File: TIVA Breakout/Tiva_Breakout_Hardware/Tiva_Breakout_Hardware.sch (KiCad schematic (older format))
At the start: 60 parts, among them U1 TM4C129E_Launchpad

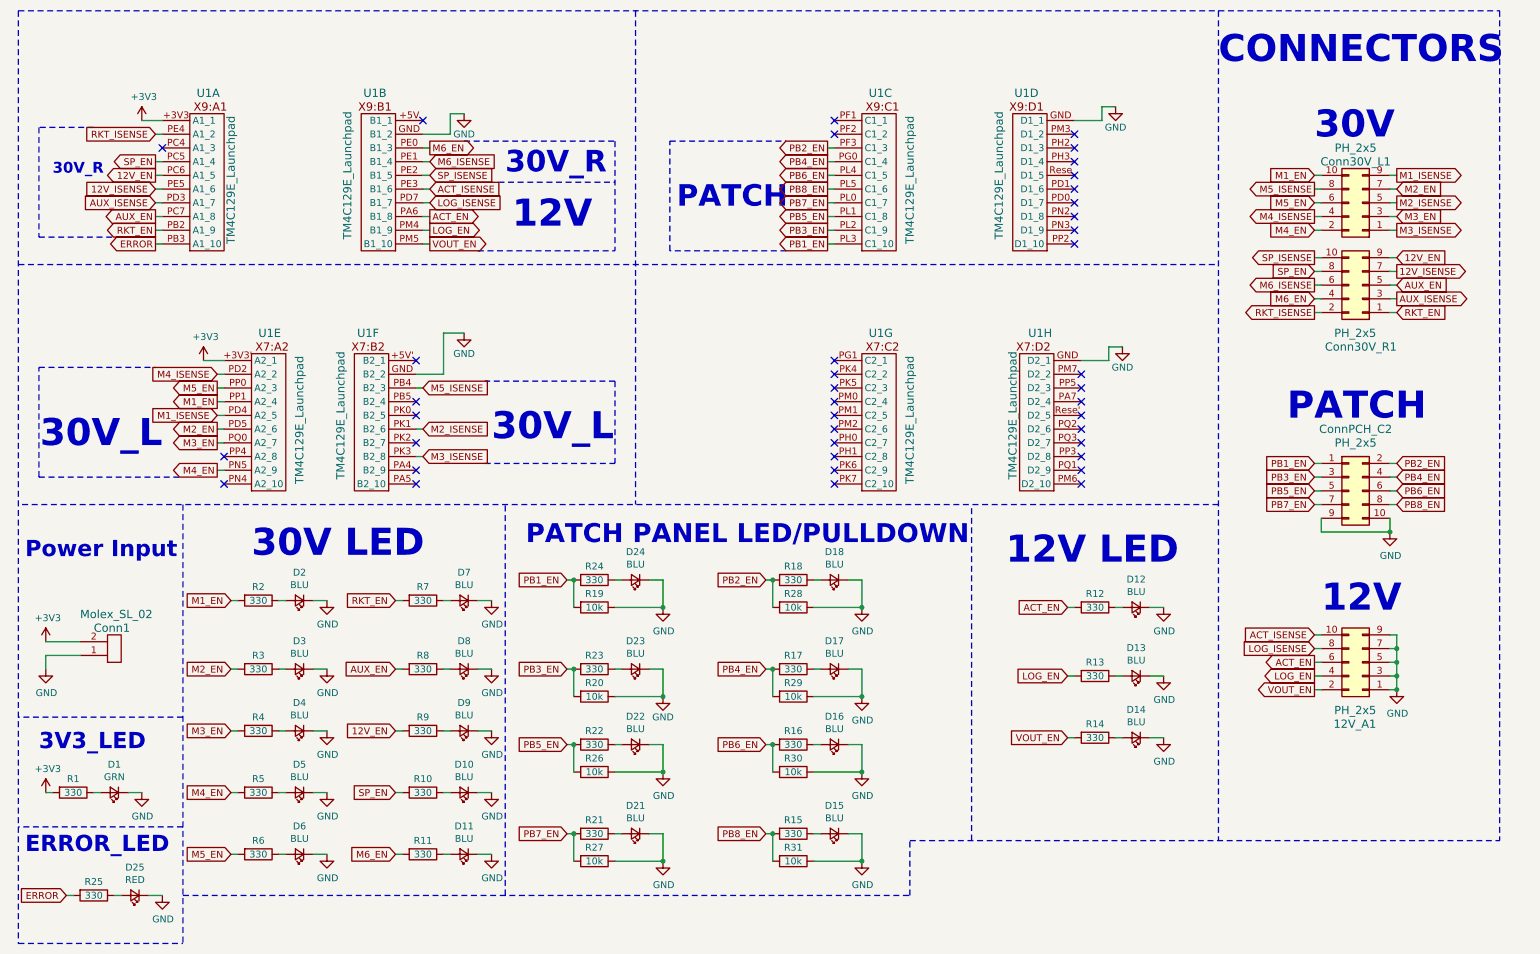
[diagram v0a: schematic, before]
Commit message: 30V connectors and part of patch panel finished
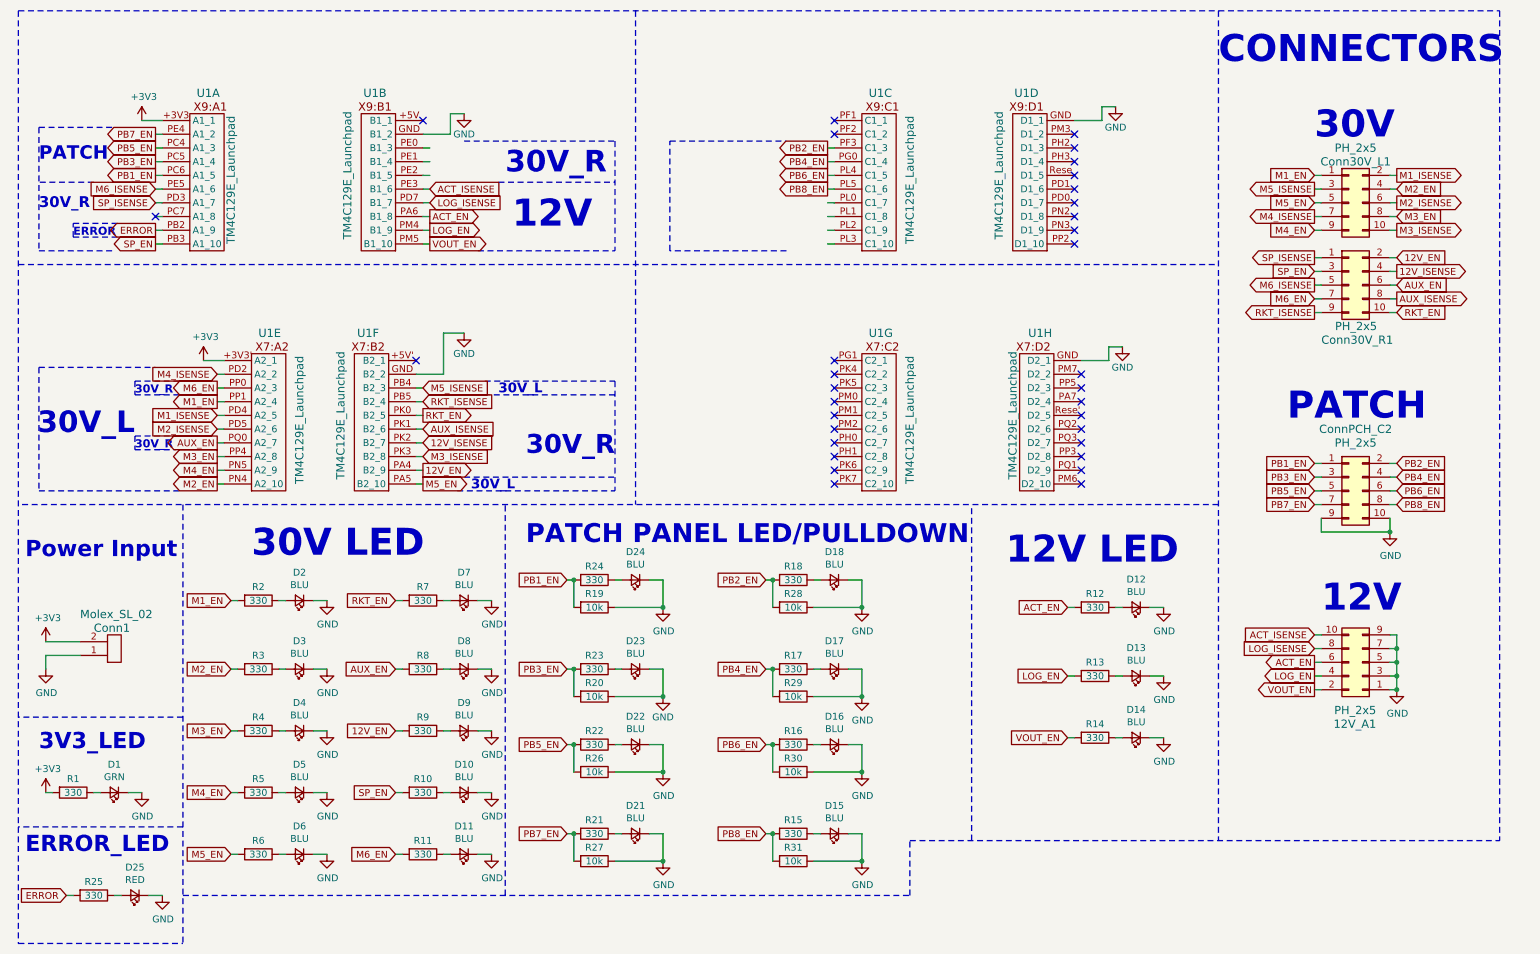
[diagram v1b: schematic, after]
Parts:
- U1: footprint MRDT_Shields:Tiva_Breakout -> Custom_Footprints:Tiva_Breakout
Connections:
- net 12V_EN: now also Conn30V_R1.2 (Pin_2), U1.PA4 (B2_9); no longer Conn30V_R1.9 (Pin_9), U1.PC6 (A1_5)
- net 12V_ISENSE: now also Conn30V_R1.4 (Pin_4), U1.PK2 (B2_7); no longer Conn30V_R1.7 (Pin_7), U1.PE5 (A1_6)
- net AUX_EN: now also Conn30V_R1.6 (Pin_6), U1.PQ0 (A2_7); no longer Conn30V_R1.5 (Pin_5), U1.PC7 (A1_8)
- net AUX_ISENSE: now also Conn30V_R1.8 (Pin_8), U1.PK1 (B2_6); no longer Conn30V_R1.3 (Pin_3), U1.PD3 (A1_7)
- net ERROR: now also U1.PB2 (A1_9); no longer U1.PB3 (A1_10)
- net M1_EN: now also Conn30V_L1.1 (Pin_1); no longer Conn30V_L1.10 (Pin_10)
- net M1_ISENSE: now also Conn30V_L1.2 (Pin_2); no longer Conn30V_L1.9 (Pin_9)
- net M2_EN: now also Conn30V_L1.4 (Pin_4), U1.PN4 (A2_10); no longer Conn30V_L1.7 (Pin_7), U1.PD5 (A2_6)
- net M2_ISENSE: now also Conn30V_L1.6 (Pin_6), U1.PD5 (A2_6); no longer Conn30V_L1.5 (Pin_5), U1.PK1 (B2_6)
- net M3_EN: now also Conn30V_L1.8 (Pin_8), U1.PP4 (A2_8); no longer Conn30V_L1.3 (Pin_3), U1.PQ0 (A2_7)
- net M3_ISENSE: now also Conn30V_L1.10 (Pin_10); no longer Conn30V_L1.1 (Pin_1)
- net M4_EN: now also Conn30V_L1.9 (Pin_9); no longer Conn30V_L1.2 (Pin_2)
- net M4_ISENSE: now also Conn30V_L1.7 (Pin_7); no longer Conn30V_L1.4 (Pin_4)
- net M5_EN: now also Conn30V_L1.5 (Pin_5), U1.PA5 (B2_10); no longer Conn30V_L1.6 (Pin_6), U1.PP0 (A2_3)
- net M5_ISENSE: now also Conn30V_L1.3 (Pin_3); no longer Conn30V_L1.8 (Pin_8)
- net M6_EN: now also Conn30V_R1.7 (Pin_7), U1.PP0 (A2_3); no longer Conn30V_R1.4 (Pin_4), U1.PE0 (B1_3)
- net M6_ISENSE: now also Conn30V_R1.5 (Pin_5), U1.PE5 (A1_6); no longer Conn30V_R1.6 (Pin_6), U1.PE1 (B1_4)
- net PB1_EN: now also U1.PC6 (A1_5); no longer U1.PL3 (C1_10)
- net PB3_EN: now also U1.PC5 (A1_4); no longer U1.PL2 (C1_9)
- net PB5_EN: now also U1.PC4 (A1_3); no longer U1.PL1 (C1_8)
- net PB7_EN: now also U1.PE4 (A1_2); no longer U1.PL0 (C1_7)
- net RKT_EN: now also Conn30V_R1.10 (Pin_10), U1.PK0 (B2_5); no longer Conn30V_R1.1 (Pin_1), U1.PB2 (A1_9)
- net RKT_ISENSE: now also Conn30V_R1.9 (Pin_9), U1.PB5 (B2_4); no longer Conn30V_R1.2 (Pin_2), U1.PE4 (A1_2)
- net SP_EN: now also Conn30V_R1.3 (Pin_3), U1.PB3 (A1_10); no longer Conn30V_R1.8 (Pin_8), U1.PC5 (A1_4)
- net SP_ISENSE: now also Conn30V_R1.1 (Pin_1), U1.PD3 (A1_7); no longer Conn30V_R1.10 (Pin_10), U1.PE2 (B1_5)
- no-connect marks 40 -> 33
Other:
- note added: "ERROR"
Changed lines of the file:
@@
 F 0 "U1" H 1750 3350 60  0000 L CNN
 F 1 "TM4C129E_Launchpad" V 2000 2250 60  0000 L CNN
-F 2 "MRDT_Shields:Tiva_Breakout" H 1700 2200 60  0001 C CNN
+F 2 "Custom_Footprints:Tiva_Breakout" H 1700 2200 60  0001 C CNN
 F 3 "" H 1700 2200 60  0001 C CNN
 	1    1700 2200
@@
 F 0 "U1" H 3350 3350 60  0000 C CNN
 F 1 "TM4C129E_Launchpad" V 3550 2750 60  0000 C CNN
-F 2 "MRDT_Shields:Tiva_Breakout" H 3200 2200 60  0001 C CNN
+F 2 "Custom_Footprints:Tiva_Breakout" H 3200 2200 60  0001 C CNN
 F 3 "" H 3200 2200 60  0001 C CNN
 	2    3200 2200
@@
 F 0 "U1" H 2200 5100 60  0000 L CNN
 F 1 "TM4C129E_Launchpad" V 2500 4000 60  0000 L CNN
-F 2 "MRDT_Shields:Tiva_Breakout" H 2150 3950 60  0001 C CNN
+F 2 "Custom_Footprints:Tiva_Breakout" H 2150 3950 60  0001 C CNN
 F 3 "" H 2150 3950 60  0001 C CNN
 	5    2150 3950
@@
 F 0 "U1" H 3300 5100 60  0000 C CNN
 F 1 "TM4C129E_Launchpad" V 3500 4500 60  0000 C CNN
-F 2 "MRDT_Shields:Tiva_Breakout" H 3150 3950 60  0001 C CNN
+F 2 "Custom_Footprints:Tiva_Breakout" H 3150 3950 60  0001 C CNN
 F 3 "" H 3150 3950 60  0001 C CNN
 	6    3150 3950
@@
 F 0 "U1" H 6650 5100 60  0000 L CNN
 F 1 "TM4C129E_Launchpad" V 6950 4000 60  0000 L CNN
-F 2 "MRDT_Shields:Tiva_Breakout" H 6600 3950 60  0001 C CNN
+F 2 "Custom_Footprints:Tiva_Breakout" H 6600 3950 60  0001 C CNN
 F 3 "" H 6600 3950 60  0001 C CNN
 	7    6600 3950
@@
 F 0 "U1" H 8100 5100 60  0000 C CNN
 F 1 "TM4C129E_Launchpad" V 8300 4500 60  0000 C CNN
-F 2 "MRDT_Shields:Tiva_Breakout" H 8000 3950 60  0001 C CNN
+F 2 "Custom_Footprints:Tiva_Breakout" H 8000 3950 60  0001 C CNN
 F 3 "" H 8000 3950 60  0001 C CNN
 	8    8000 3950
@@
 L Connector_Generic:Conn_02x05_Odd_Even Conn30V_L1
 U 1 1 5DCE1DDF
-P 10250 1850
-F 0 "Conn30V_L1" H 10300 1550 60  0000 C CNN
-F 1 "PH_2x5" H 10300 1450 60  0000 C CNN
-F 2 "MRDT_Connectors:JTAG_ARM_Connector_10_Pin" H 10250 2150 60  0001 C CNN
-F 3 "" H 10250 2150 60  0001 C CNN
-	1    10250 1850
-	-1   0    0    1
+P 10150 1850
+F 0 "Conn30V_L1" H 10200 2150 60  0000 C CNN
+F 1 "PH_2x5" H 10200 2250 60  0000 C CNN
+F 2 "MRDT_Connectors:JTAG_ARM_Connector_10_Pin" H 10150 2150 60  0001 C CNN
+F 3 "" H 10150 2150 60  0001 C CNN
+	1    10150 1850
+	1    0    0    -1
 $EndComp
 $Comp
 L Connector_Generic:Conn_02x05_Odd_Even Conn30V_R1
 U 1 1 5DCE5C02
-P 10250 2450
-F 0 "Conn30V_R1" H 10000 2900 60  0000 L CNN
-F 1 "PH_2x5" H 10150 2800 60  0000 L CNN
-F 2 "MRDT_Connectors:JTAG_ARM_Connector_10_Pin" H 10250 2750 60  0001 C CNN
-F 3 "" H 10250 2750 60  0001 C CNN
-	1    10250 2450
-	-1   0    0    1
+P 10150 2450
+F 0 "Conn30V_R1" H 9950 2050 60  0000 L CNN
+F 1 "PH_2x5" H 10050 2150 60  0000 L CNN
+F 2 "MRDT_Connectors:JTAG_ARM_Connector_10_Pin" H 10150 2750 60  0001 C CNN
+F 3 "" H 10150 2750 60  0001 C CNN
+	1    10150 2450
+	1    0    0    -1
 $EndComp
 Wire Wire Line
@@
 F 0 "U1" H 8100 3350 60  0000 C CNN
 F 1 "TM4C129E_Launchpad" V 8300 2750 60  0000 C CNN
-F 2 "MRDT_Shields:Tiva_Breakout" H 7950 2200 60  0001 C CNN
+F 2 "Custom_Footprints:Tiva_Breakout" H 7950 2200 60  0001 C CNN
 F 3 "" H 7950 2200 60  0001 C CNN
 	4    7950 2200
@@
 Wire Wire Line
 	3600 1200 3600 1350
-Text GLabel 1450 1750 0    50   Input ~ 0
+Text GLabel 3400 3600 2    50   Input ~ 0
 12V_ISENSE
-Text GLabel 1450 1850 0    50   Input ~ 0
+Text GLabel 3400 3500 2    50   Input ~ 0
 AUX_ISENSE
-Text GLabel 1450 1350 0    50   Input ~ 0
+Text GLabel 3400 3300 2    50   Input ~ 0
 RKT_ISENSE
-Text GLabel 1450 2050 0    50   Output ~ 0
+Text GLabel 3400 3400 2    50   Output ~ 0
 RKT_EN
-Text GLabel 1450 1950 0    50   Output ~ 0
+Text GLabel 1900 3600 0    50   Output ~ 0
 AUX_EN
-Text GLabel 1450 1650 0    50   Output ~ 0
+Text GLabel 3400 3800 2    50   Output ~ 0
 12V_EN
 Text GLabel 10500 2250 2    50   Input ~ 0
@@
 Wire Wire Line
 	10450 1650 10500 1650
-Text GLabel 1450 1550 0    50   Output ~ 0
+Text GLabel 1450 2150 0    50   Output ~ 0
 SP_EN
-Text GLabel 3450 1650 2    50   Input ~ 0
+Text GLabel 1450 1850 0    50   Input ~ 0
 SP_ISENSE
 $Comp
@@
 Wire Wire Line
 	10450 2250 10500 2250
-Text GLabel 3450 1450 2    50   Output ~ 0
+Text GLabel 1900 3200 0    50   Output ~ 0
 M6_EN
-Text GLabel 3450 1550 2    50   Input ~ 0
+Text GLabel 1450 1750 0    50   Input ~ 0
 M6_ISENSE
-Text GLabel 1900 3200 0    50   Output ~ 0
+Text GLabel 3400 3900 2    50   Output ~ 0
 M5_EN
 Text GLabel 3400 3200 2    50   Input ~ 0
@@
 Text GLabel 1900 3100 0    50   Input ~ 0
 M4_ISENSE
-Text GLabel 1900 3600 0    50   Output ~ 0
+Text GLabel 1900 3700 0    50   Output ~ 0
 M3_EN
 Text GLabel 3400 3700 2    50   Input ~ 0
@@
 Text GLabel 1900 3300 0    50   Output ~ 0
 M1_EN
-Text GLabel 3400 3500 2    50   Input ~ 0
+Text GLabel 1900 3500 0    50   Input ~ 0
 M2_ISENSE
-Text GLabel 1900 3500 0    50   Output ~ 0
+Text GLabel 1900 3900 0    50   Output ~ 0
 M2_EN
 Wire Wire Line
@@
 Wire Wire Line
 	3400 3200 3350 3200
-Text Notes 3900 3600 0    197  ~ 39
-30V_L
-Wire Notes Line
-	3850 3750 4800 3750
-Wire Notes Line
-	4800 3150 3850 3150
-Text Notes 1500 3650 2    197  ~ 39
+Text Notes 4150 3700 0    138  ~ 28
+30V_R
+Wire Notes Line
+	4800 3250 3850 3250
+Text Notes 1300 3550 2    157  ~ 31
 30V_L
 Wire Wire Line
@@
 F 0 "U1" H 6650 3350 60  0000 L CNN
 F 1 "TM4C129E_Launchpad" V 6950 2250 60  0000 L CNN
-F 2 "MRDT_Shields:Tiva_Breakout" H 6600 2200 60  0001 C CNN
+F 2 "Custom_Footprints:Tiva_Breakout" H 6600 2200 60  0001 C CNN
 F 3 "" H 6600 2200 60  0001 C CNN
 	3    6600 2200
@@
 Wire Wire Line
 	3350 3700 3400 3700
-NoConn ~ 1500 1450
-Text Notes 700  1650 0    79   ~ 16
+Text Notes 600  1900 0    79   ~ 16
 30V_R
 Wire Notes Line
-	1000 1300 600  1300
-Wire Notes Line
-	600  1300 600  2100
-Wire Notes Line
-	600  2100 1150 2100
+	600  2200 1150 2200
 Wire Notes Line
 	3700 1400 4800 1400
-Wire Notes Line
-	4800 3150 4800 3750
-NoConn ~ 3350 3300
-NoConn ~ 3350 3400
-NoConn ~ 3350 3600
-NoConn ~ 3350 3800
-NoConn ~ 3350 3900
-NoConn ~ 1950 3900
-NoConn ~ 1950 3700
-Wire Notes Line
-	600  3850 600  3050
 $Comp
 L Device:R R12
@@
 Text Notes 7650 4500 0    197  ~ 39
 12V LED
-Text GLabel 6350 2150 0    50   Output ~ 0
-PB1_EN
 Text GLabel 6350 1450 0    50   Output ~ 0
 PB2_EN
-Text GLabel 6350 2050 0    50   Output ~ 0
-PB3_EN
 Text GLabel 6350 1550 0    50   Output ~ 0
 PB4_EN
-Text GLabel 6350 1950 0    50   Output ~ 0
-PB5_EN
 Text GLabel 6350 1650 0    50   Output ~ 0
 PB6_EN
-Text GLabel 6350 1850 0    50   Output ~ 0
-PB7_EN
 Text GLabel 6350 1750 0    50   Output ~ 0
 PB8_EN
@@
 Text GLabel 5900 6450 0    50   Input ~ 0
 PB8_EN
-Text GLabel 1450 2150 0    50   Output ~ 0
+Text GLabel 1450 2050 0    50   Output ~ 0
 ERROR
 Wire Wire Line
@@
 Wire Notes Line
 	4950 450  4950 4050
-Text Notes 5250 1900 0    157  ~ 31
+Text Notes 600  1550 0    98   ~ 20
 PATCH
 Wire Notes Line
@@
 Wire Notes Line
 	6950 6500 11250 6500
-Wire Notes Line
-	600  3850 1650 3850
 Wire Notes Line
 	600  3050 1450 3050
@@
 Wire Notes Line
 	5200 1400 6050 1400
+Wire Wire Line
+	1950 3700 1900 3700
+Wire Wire Line
+	1950 3900 1900 3900
+Wire Notes Line
+	600  3950 1650 3950
+Wire Wire Line
+	3350 3900 3400 3900
+Wire Wire Line
+	3350 3300 3400 3300
+Wire Wire Line
+	3350 3400 3400 3400
+Wire Wire Line
+	3350 3600 3400 3600
+Wire Wire Line
+	3350 3800 3400 3800
+Wire Wire Line
+	1500 1450 1450 1450
+Wire Notes Line
+	600  3050 600  3950
+Wire Notes Line
+	600  1300 600  2200
+Wire Notes Line
+	850  2100 850  2000
+Text Notes 850  2100 0    59   ~ 12
+ERROR
+Wire Notes Line
+	850  2000 1200 2000
+Wire Notes Line
+	850  2100 1200 2100
+Wire Notes Line
+	1300 3150 1300 3250
+Wire Notes Line
+	1300 3550 1300 3650
+Text Notes 1300 3250 0    59   ~ 12
+30V_R
+Text Notes 1300 3650 0    59   ~ 12
+30V_R
+Wire Notes Line
+	1300 3250 1650 3250
+Wire Notes Line
+	1300 3150 1650 3150
+Wire Notes Line
+	1300 3550 1600 3550
+Wire Notes Line
+	1300 3650 1600 3650
+Wire Notes Line
+	3700 3850 4800 3850
+Wire Notes Line
+	3850 3150 4800 3150
+Wire Notes Line
+	3650 3950 4800 3950
+Wire Notes Line
+	4800 3150 4800 3950
+Text Notes 3950 3250 0    71   ~ 14
+30V_L
+Text Notes 3750 3950 0    71   ~ 14
+30V_L
+Wire Notes Line
+	1000 1700 600  1700
+NoConn ~ 1450 1950
+Text GLabel 1450 1350 0    50   Output ~ 0
+PB7_EN
+Text GLabel 1450 1450 0    50   Output ~ 0
+PB5_EN
+Text GLabel 1450 1550 0    50   Output ~ 0
+PB3_EN
+Text GLabel 1450 1650 0    50   Output ~ 0
+PB1_EN
+Wire Notes Line
+	600  1300 1150 1300
 $EndSCHEMATC
